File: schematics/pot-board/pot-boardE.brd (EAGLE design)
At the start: 124.4 x 41.9 mm, 18 parts, among them J3 POWER_JACKPTH_LOCK, U1 SPARKFUN_PRO_MICRO, U2 DC-DC-STEP-DOWN-LM2596

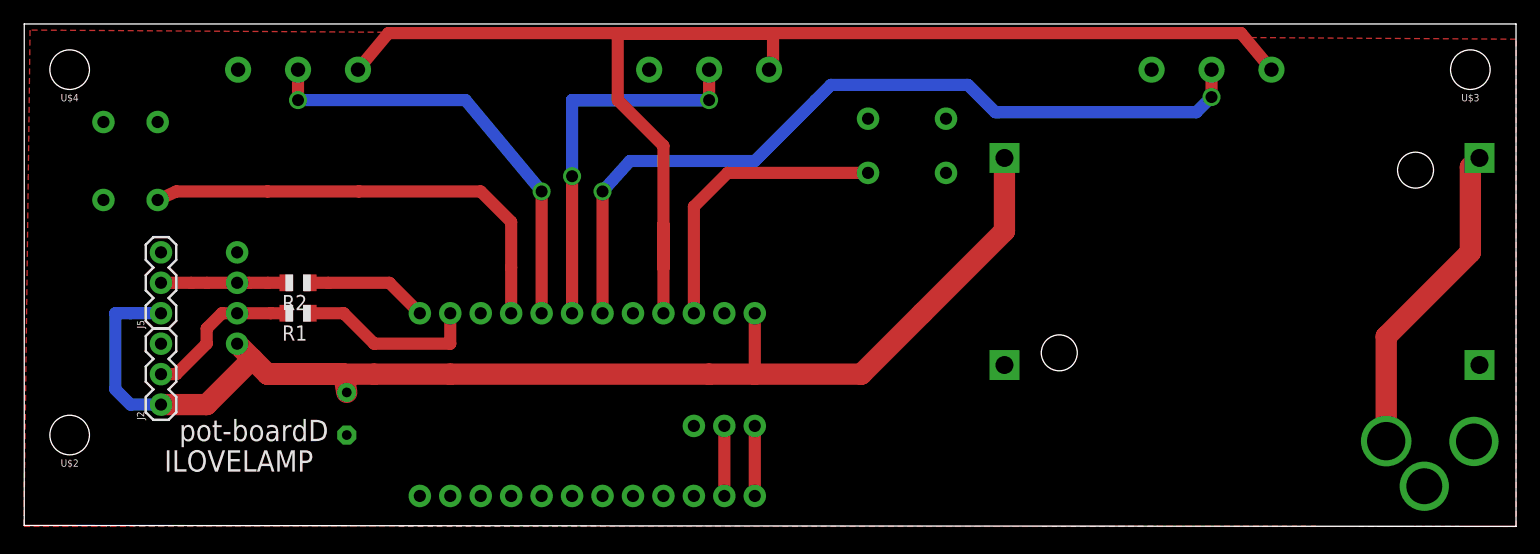
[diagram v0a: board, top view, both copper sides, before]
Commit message: added variations up to woodArc1 using pot-boardE
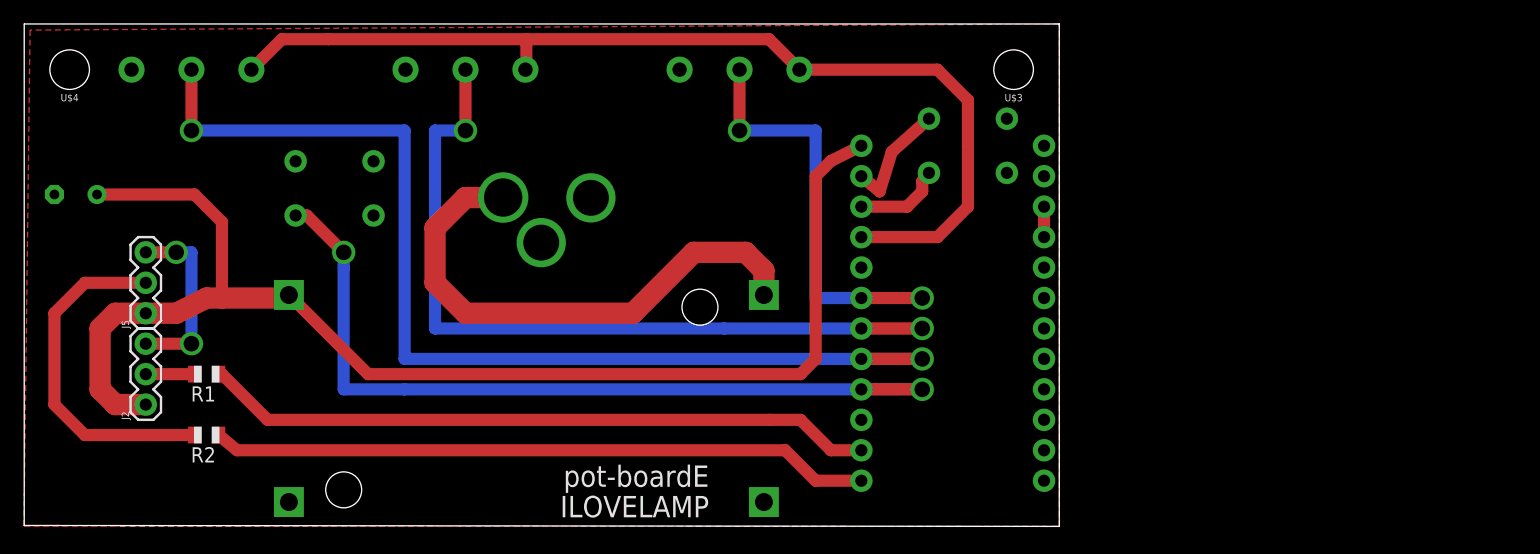
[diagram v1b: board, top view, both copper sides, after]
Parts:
- removed J1: (no value), SparkFun-Connectors:1X04
- removed J4: (no value), SparkFun-Connectors:1X03
- removed U$2: (no value), SparkFun-Hardware:STAND-OFF
- moved J3 76.4 mm to (53.8, 27.4)
- moved U2 60.8 mm to (41.9, 10.7)
- moved R5 39.4 mm to (59.7, 38.1)
- moved U$3 38.1 mm to (82.5, 38.1)
- moved U1 30.5 mm to (77.5, 19.1), turned to 0 degrees
- moved C2 29.1 mm to (4.32, 27.7), turned to 0 degrees
- moved R4 20.3 mm to (36.8, 38.1)
- moved S1 17.2 mm to (25.9, 28.2), turned to 180 degrees
- moved R2 14.8 mm to (15.2, 7.62)
- moved R1 9.16 mm to (15.2, 12.7)
- moved R3 8.89 mm to (14.0, 38.1)
- moved S4 5.08 mm to (78.7, 31.8)
- moved J2 1.27 mm to (10.2, 10.2)
- moved J5 1.27 mm to (10.2, 17.8)
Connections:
- removed net N$3: J4.2, U1.2
- removed net N$4: J4.3, U1.1
- net GND: no longer J1.4, J4.1
- net LED1O: no longer J1.3
- net LED2O: no longer J1.2
- net VIN: no longer J1.1
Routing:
- net VCC: track 166.3 -> 84.4 mm
- net A0: track 36.6 -> 90.2 mm
- net LED1: track 10.2 -> 55.1 mm
- net LED2: track 15.3 -> 56.2 mm
- net BUTT1: track 38.3 -> 70.1 mm, vias 0 -> 2
- net A2: track 68.5 -> 39.4 mm
- net GND: track 0.00 -> 27.4 mm, vias 0 -> 2
- net LED1O: track 10.4 -> 29.0 mm
- net N$1: track 26.8 -> 44.6 mm
- net RESET: track 24.6 -> 7.35 mm
- net A1: track 54.6 -> 69.9 mm
- net LED2O: track 13.3 -> 4.08 mm
- net N$4: track 5.84 -> 0.00 mm
- net N$3: track 5.84 -> 0.00 mm
- net VIN: track 116.6 -> 113.7 mm
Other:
- board size 124.4 x 41.9 mm -> 86.3 x 41.9 mm
- board text added: "pot-boardE"
- board text removed: "pot-boardD"
